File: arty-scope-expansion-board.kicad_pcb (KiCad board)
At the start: 4 copper layers, 109 x 86 mm, 20 parts, among them J1 PMOD_A, J2 PMOD_B, J3 PMOD_C, J4 PMOD_D, U1 AD9288, U2 74LS374, U3 74LS374

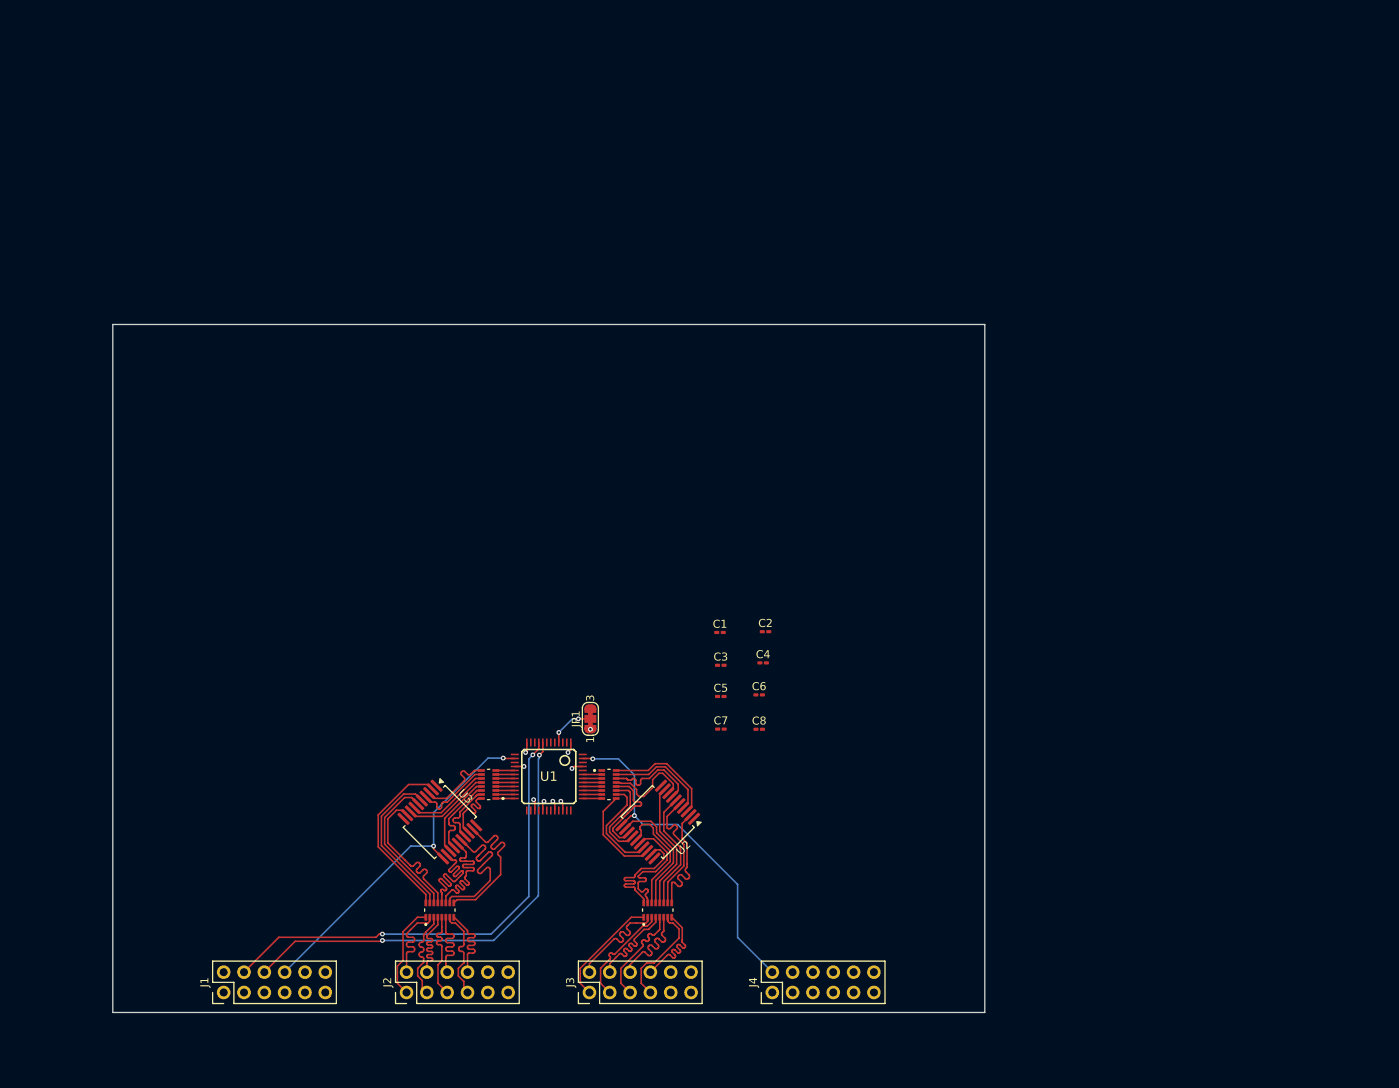
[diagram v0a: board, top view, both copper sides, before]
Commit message: [feat] Added footprints to all A channel elements
TVS diode still doesn't have correct footprint or model. Find one on
LCSC.
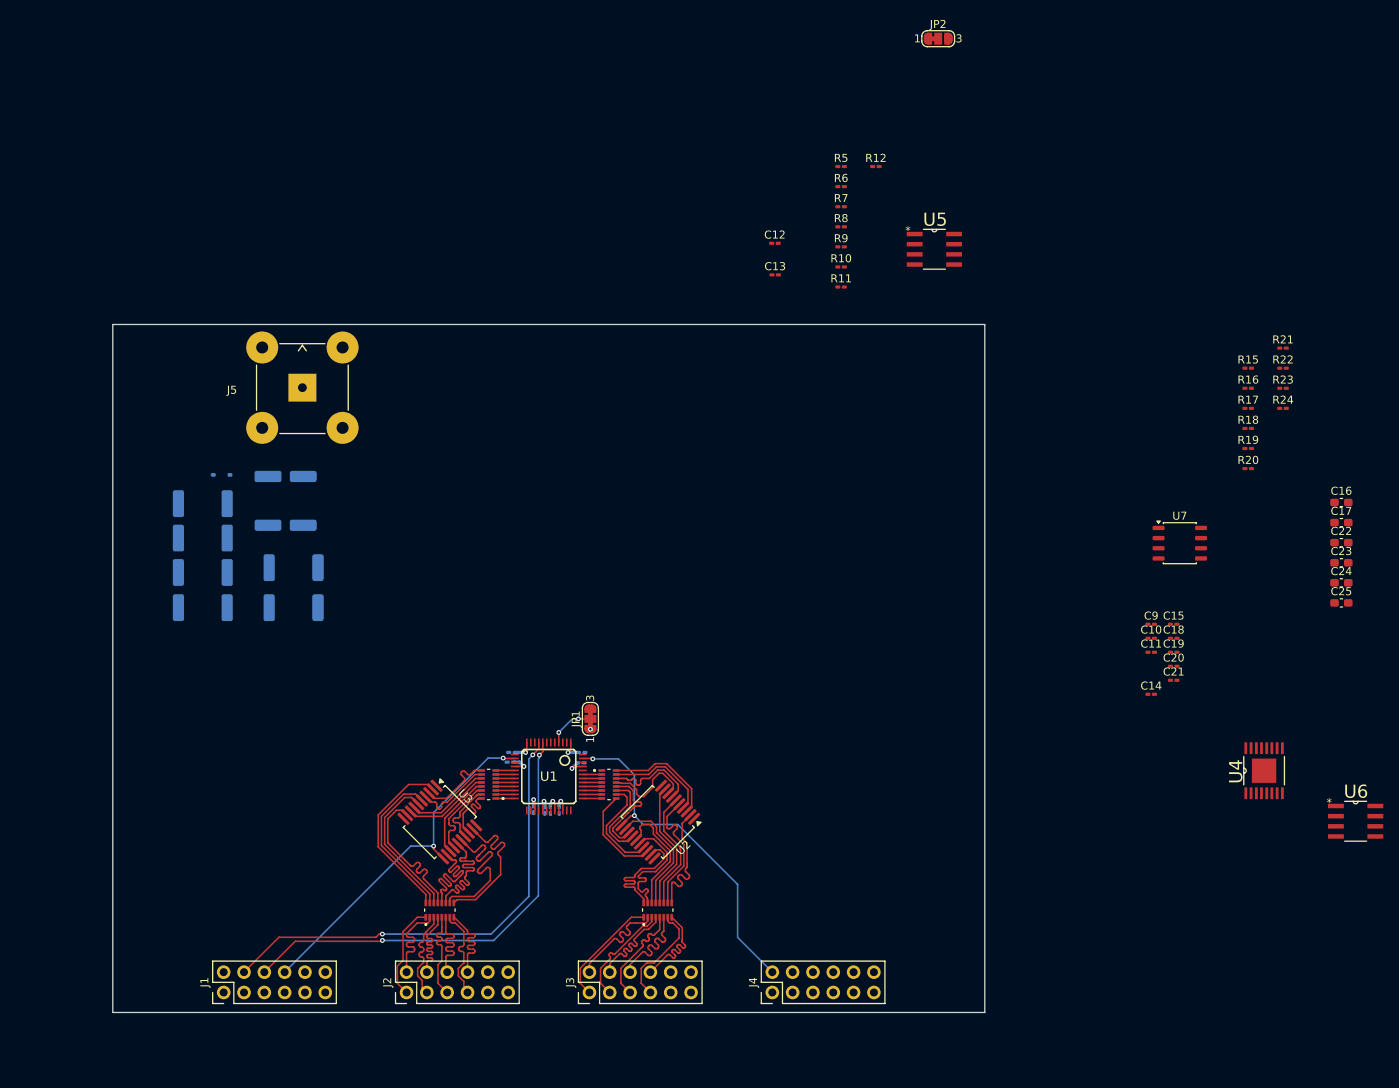
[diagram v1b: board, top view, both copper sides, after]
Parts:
- added C10: 1n, Capacitor_SMD:C_0201_0603Metric_Pad0.64x0.40mm_HandSolder, F.Cu at (245.3, 76.2)
- added C11: 1n, Capacitor_SMD:C_0201_0603Metric_Pad0.64x0.40mm_HandSolder, F.Cu at (245.3, 78.0)
- added C12: 10u, Capacitor_SMD:C_0201_0603Metric_Pad0.64x0.40mm_HandSolder, F.Cu at (198.3, 26.9)
- added C13: 100n, Capacitor_SMD:C_0201_0603Metric_Pad0.64x0.40mm_HandSolder, F.Cu at (198.3, 30.8)
- added C14: 100n, Capacitor_SMD:C_0201_0603Metric_Pad0.64x0.40mm_HandSolder, F.Cu at (245.3, 83.2)
- added C15: 10u, Capacitor_SMD:C_0201_0603Metric_Pad0.64x0.40mm_HandSolder, F.Cu at (248.1, 74.5)
- added C16: 100n, Capacitor_SMD:C_0603_1608Metric_Pad1.08x0.95mm_HandSolder, F.Cu at (269.1, 59.3)
- added C17: 100n, Capacitor_SMD:C_0603_1608Metric_Pad1.08x0.95mm_HandSolder, F.Cu at (269.1, 61.8)
- added C18: 47p, Capacitor_SMD:C_0201_0603Metric_Pad0.64x0.40mm_HandSolder, F.Cu at (248.1, 76.2)
- added C19: 10p, Capacitor_SMD:C_0201_0603Metric_Pad0.64x0.40mm_HandSolder, F.Cu at (248.1, 78.0)
- added C20: 100n, Capacitor_SMD:C_0201_0603Metric_Pad0.64x0.40mm_HandSolder, F.Cu at (248.1, 79.7)
- added C21: 10u, Capacitor_SMD:C_0201_0603Metric_Pad0.64x0.40mm_HandSolder, F.Cu at (248.1, 81.5)
- added C22: 10u, Capacitor_SMD:C_0603_1608Metric_Pad1.08x0.95mm_HandSolder, F.Cu at (269.1, 64.3)
- added C23: 100n, Capacitor_SMD:C_0603_1608Metric_Pad1.08x0.95mm_HandSolder, F.Cu at (269.1, 66.8)
- added C24: 10u, Capacitor_SMD:C_0603_1608Metric_Pad1.08x0.95mm_HandSolder, F.Cu at (269.1, 69.3)
- added C25: 100n, Capacitor_SMD:C_0603_1608Metric_Pad1.08x0.95mm_HandSolder, F.Cu at (269.1, 71.8)
- added C9: 100n, Capacitor_SMD:C_0201_0603Metric_Pad0.64x0.40mm_HandSolder, F.Cu at (245.3, 74.5)
- added D3: SD24C-01F, Diode_SMD:D_SOD-323, B.Cu at (129.1, 55.8)
- added J5: Conn_Coaxial, Connector_Coaxial:BNC_TEConnectivity_1478035_Horizontal, F.Cu at (139.2, 44.9)
- added JP2: Jumper_3_Bridged12, Jumper:SolderJumper-3_P1.3mm_Bridged12_RoundedPad1.0x1.5mm_NumberLabels, F.Cu at (218.7, 1.27)
- added R1: 11, Resistor_SMD:R_2512_6332Metric_Pad1.40x3.35mm_HandSolder, B.Cu at (139.3, 59.0)
- added R10: Rt/2, Resistor_SMD:R_0201_0603Metric_Pad0.64x0.40mm_HandSolder, F.Cu at (206.5, 29.8)
- added R11: 499, Resistor_SMD:R_0201_0603Metric_Pad0.64x0.40mm_HandSolder, F.Cu at (206.5, 32.3)
- added R12: 499, Resistor_SMD:R_0201_0603Metric_Pad0.64x0.40mm_HandSolder, F.Cu at (210.9, 17.3)
- added R13: 11, Resistor_SMD:R_2512_6332Metric_Pad1.40x3.35mm_HandSolder, B.Cu at (134.9, 59.0)
- added R14: 222, Resistor_SMD:R_2512_6332Metric_Pad1.40x3.35mm_HandSolder, B.Cu at (126.8, 59.4)
- added R15: 499, Resistor_SMD:R_0201_0603Metric_Pad0.64x0.40mm_HandSolder, F.Cu at (257.4, 42.5)
- added R16: 499, Resistor_SMD:R_0201_0603Metric_Pad0.64x0.40mm_HandSolder, F.Cu at (257.4, 45.0)
- added R17: 499, Resistor_SMD:R_0201_0603Metric_Pad0.64x0.40mm_HandSolder, F.Cu at (257.4, 47.5)
- added R18: 499, Resistor_SMD:R_0201_0603Metric_Pad0.64x0.40mm_HandSolder, F.Cu at (257.4, 50.0)
- added R19: 100, Resistor_SMD:R_0201_0603Metric_Pad0.64x0.40mm_HandSolder, F.Cu at (257.4, 52.5)
- added R2: 222, Resistor_SMD:R_2512_6332Metric_Pad1.40x3.35mm_HandSolder, B.Cu at (126.8, 72.4)
- added R20: 100, Resistor_SMD:R_0201_0603Metric_Pad0.64x0.40mm_HandSolder, F.Cu at (257.4, 55.0)
- added R21: 2.61k, Resistor_SMD:R_0201_0603Metric_Pad0.64x0.40mm_HandSolder, F.Cu at (261.8, 40.0)
- added R22: 10k, Resistor_SMD:R_0201_0603Metric_Pad0.64x0.40mm_HandSolder, F.Cu at (261.8, 42.5)
- added R23: 49.9, Resistor_SMD:R_0201_0603Metric_Pad0.64x0.40mm_HandSolder, F.Cu at (261.8, 45.0)
- added R24: 49.9, Resistor_SMD:R_0201_0603Metric_Pad0.64x0.40mm_HandSolder, F.Cu at (261.8, 47.5)
- added R25: 222, Resistor_SMD:R_2512_6332Metric_Pad1.40x3.35mm_HandSolder, B.Cu at (126.8, 63.7)
- added R26: 222, Resistor_SMD:R_2512_6332Metric_Pad1.40x3.35mm_HandSolder, B.Cu at (126.8, 68.0)
- added R3: 499, Resistor_SMD:R_2512_6332Metric_Pad1.40x3.35mm_HandSolder, B.Cu at (138.1, 72.4)
- added R4: 55.6, Resistor_SMD:R_2512_6332Metric_Pad1.40x3.35mm_HandSolder, B.Cu at (138.1, 67.4)
- added R5: 100, Resistor_SMD:R_0201_0603Metric_Pad0.64x0.40mm_HandSolder, F.Cu at (206.5, 17.3)
- added R6: 100, Resistor_SMD:R_0201_0603Metric_Pad0.64x0.40mm_HandSolder, F.Cu at (206.5, 19.8)
- added R7: 499, Resistor_SMD:R_0201_0603Metric_Pad0.64x0.40mm_HandSolder, F.Cu at (206.5, 22.3)
- added R8: 499, Resistor_SMD:R_0201_0603Metric_Pad0.64x0.40mm_HandSolder, F.Cu at (206.5, 24.8)
- added R9: Rt, Resistor_SMD:R_0201_0603Metric_Pad0.64x0.40mm_HandSolder, F.Cu at (206.5, 27.3)
- added U4: AD8370AREZ-RL7, inzynierka.Library:SOP65P640X120-17N, F.Cu at (259.4, 92.8)
- added U5: AD8132ARZ, inzynierka.Library:SOIC127P600X175-8N, F.Cu at (218.2, 27.6)
- added U6: AD8132ARZ, inzynierka.Library:SOIC127P600X175-8N, F.Cu at (270.9, 99.1)
- added U7: MCP4822, Package_SO:JEITA_SOIC-8_3.9x4.9mm_P1.27mm, F.Cu at (248.9, 64.3)
- C1, C2, C3, C4, C5, C6, C7, C8: moved to B.Cu
- JP1: value Jumper_3_Bridged12 -> DFS Select
- moved C2 34.9 mm to (170.2, 97.7), turned to 90 degrees
- moved C4 34.0 mm to (168.1, 97.6), turned to 90 degrees
- moved C6 32.2 mm to (165.2, 91.7)
- moved C1 29.9 mm to (171.3, 97.7), turned to 90 degrees
- moved C3 28.5 mm to (169.5, 97.7), turned to 90 degrees
- moved C5 27.0 mm to (165.4, 90.5)
- moved C8 22.7 mm to (174.0, 91.8), turned to 180 degrees
- moved C7 17.7 mm to (174.1, 90.5), turned to 180 degrees
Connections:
- C1 pad 1: VDD -> +3.3VCC
- C2 pad 1: VDD -> +3.3VCC
- C3 pad 1: VDD -> +3.3VCC
- C4 pad 1: VDD -> +3.3VCC
- C5 pad 1: VDD -> +3.3VCC
- C6 pad 1: VDD -> +3.3VCC
- C7 pad 1: VDD -> +3.3VCC
- C8 pad 1: VDD -> +3.3VCC
- J1 pad 1: unconnected-(J1-Pin_1-Pad1) -> PGA_CLK_A
- J1 pad 11: VDD -> +3.3VCC
- J1 pad 12: VDD -> +3.3VCC
- J1 pad 3: unconnected-(J1-Pin_3-Pad3) -> PGA_DATA_A
- J1 pad 5: unconnected-(J1-Pin_5-Pad5) -> PGA_LATCH_A
- J2 pad 11: VDD -> +3.3VCC
- J2 pad 12: VDD -> +3.3VCC
- J3 pad 11: VDD -> +3.3VCC
- J3 pad 12: VDD -> +3.3VCC
- J4 pad 1: unconnected-(J4-Pin_1-Pad1) -> PGA_CLK_B
- J4 pad 11: VDD -> +3.3VCC
- J4 pad 12: VDD -> +3.3VCC
- J4 pad 3: unconnected-(J4-Pin_3-Pad3) -> PGA_DATA_B
- J4 pad 4: unconnected-(J4-Pin_4-Pad4) -> DAC_CS
- J4 pad 5: unconnected-(J4-Pin_5-Pad5) -> PGA_LATCH_B
- J4 pad 6: unconnected-(J4-Pin_6-Pad6) -> DAC_SDI
- J4 pad 7: unconnected-(J4-Pin_7-Pad7) -> DAC_LDAC
- J4 pad 8: unconnected-(J4-Pin_8-Pad8) -> DAC_SCK
- U1 pad 13: VDD -> +3.3VCC
- U1 pad 15: VDD -> +3.3VCC
- U1 pad 2: unconnected-(U1-AINA-Pad2) -> +AINA
- U1 pad 28: VDD -> +3.3VCC
- U1 pad 3: unconnected-(U1-/AINA-Pad3) -> -AINA
- U1 pad 30: VDD -> +3.3VCC
- U1 pad 31: VDD -> +3.3VCC
- U1 pad 33: VDD -> +3.3VCC
- U1 pad 46: VDD -> +3.3VCC
- U1 pad 48: VDD -> +3.3VCC
- U1 pad 5: unconnected-(U1-REFINA-Pad5) -> REFOUT
- U1 pad 6: unconnected-(U1-REFOUT-Pad6) -> REFOUT
- U1 pad 7: unconnected-(U1-REFINB-Pad7) -> REFOUT
- U2 pad 20: +3.3V -> +3.3VCC
- U3 pad 20: +3.3V -> +3.3VCC
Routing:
- net GND: track 10.6 -> 18.8 mm

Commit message: [feat] Started routing A channel input traces
Input 50 Ohm traces still needs routing. Anty aliasing filter needs
checking if values are correct with some simulation software. Still no
power planes. Serial signals for PGA/VGA and DAC needs logic level
shifters from 3.3V FPGA to 5V signals.
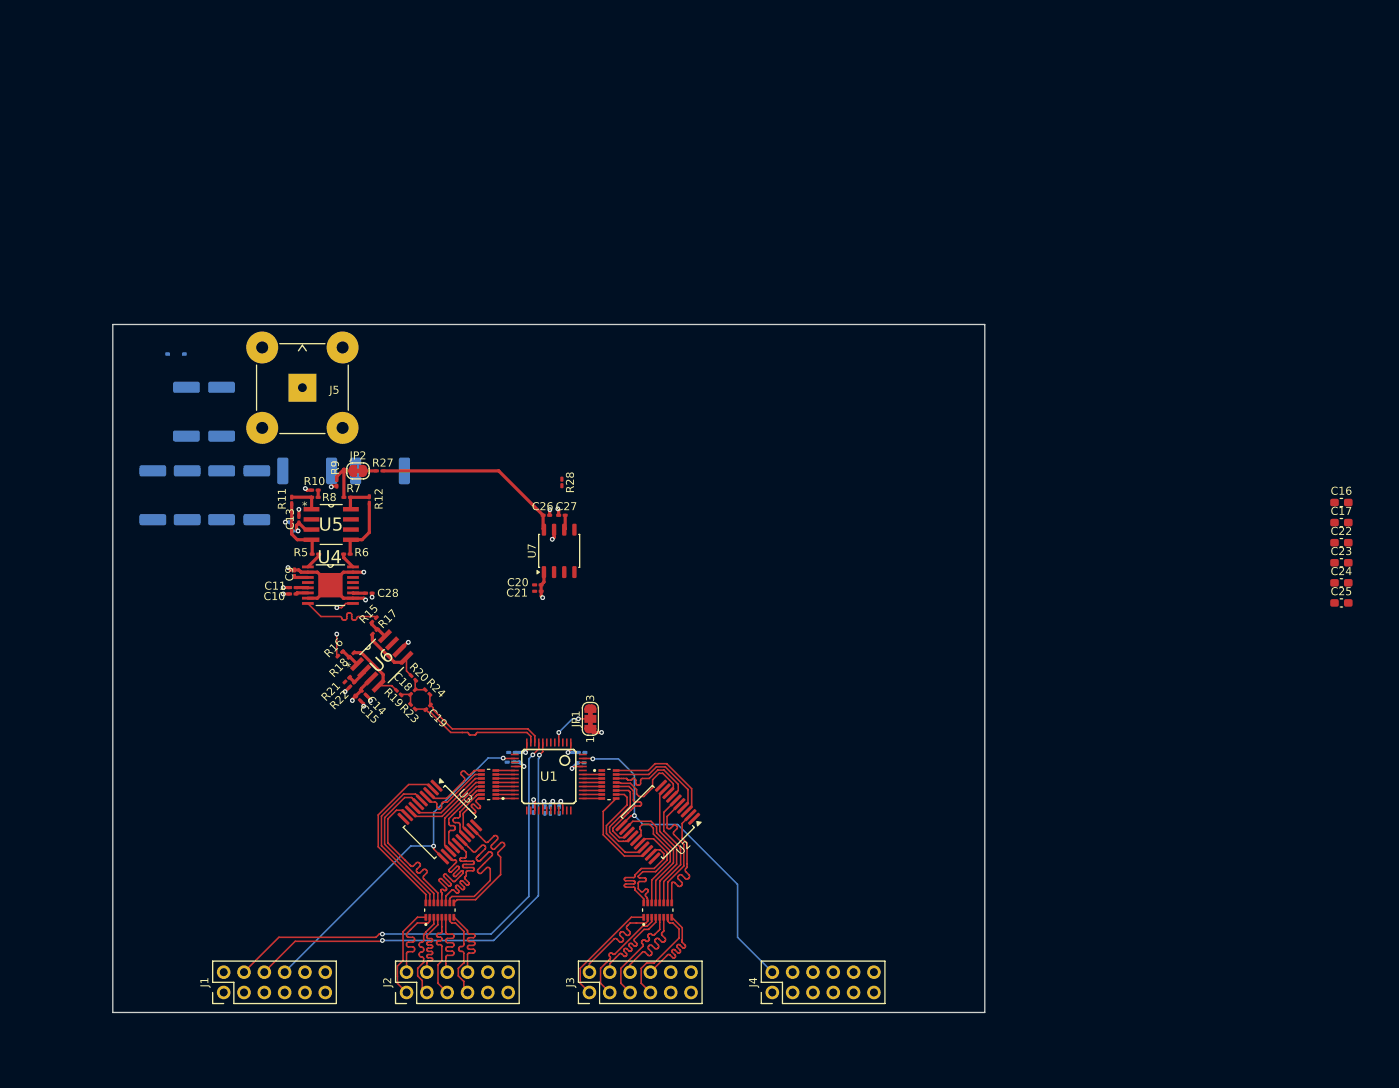
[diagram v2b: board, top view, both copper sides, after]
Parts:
- added C26: 1n, Capacitor_SMD:C_0201_0603Metric_Pad0.64x0.40mm_HandSolder, F.Cu at (169.7, 60.9)
- added C27: 1n, Capacitor_SMD:C_0201_0603Metric_Pad0.64x0.40mm_HandSolder, F.Cu at (171.6, 60.9)
- added C28: 1n, Capacitor_SMD:C_0201_0603Metric_Pad0.64x0.40mm_HandSolder, F.Cu at (147.5, 70.6)
- added R27: 20k, Resistor_SMD:R_0201_0603Metric_Pad0.64x0.40mm_HandSolder, F.Cu at (148.9, 55.3)
- added R28: 20k, Resistor_SMD:R_0201_0603Metric_Pad0.64x0.40mm_HandSolder, F.Cu at (171.6, 56.7)
- C12: moved to B.Cu
- JP2: value Jumper_3_Bridged12 -> Jumper_2_Bridged; footprint Jumper:SolderJumper-3_P1.3mm_Bridged12_RoundedPad1.0x1.5mm_NumberLabels -> Jumper:SolderJumper-2_P1.3mm_Bridged_RoundedPad1.0x1.5mm
- R10: value Rt/2 -> 27.8
- R9: value Rt -> 55.6
- moved R21 124.1 mm to (144.8, 81.4), turned to -135 degrees
- moved U6 123.4 mm to (149.1, 79.1), turned to 45 degrees
- moved R22 122.9 mm to (145.4, 82.0), turned to 45 degrees
- moved U4 119.0 mm to (142.7, 69.6), turned to 0 degrees
- moved R16 118.3 mm to (143.9, 78.2), turned to 45 degrees
- moved R23 115.8 mm to (153.0, 84.8), turned to -45 degrees
- moved R18 115.6 mm to (145.3, 78.3), turned to 45 degrees
- moved R15 113.7 mm to (148.2, 73.9), turned to -135 degrees
- moved R17 112.7 mm to (148.2, 75.4), turned to 45 degrees
- moved R24 112.7 mm to (154.8, 82.9), turned to -45 degrees
- moved R19 110.5 mm to (151.2, 83.0), turned to -45 degrees
- moved C11 107.6 mm to (138.0, 69.9)
- moved R20 107.6 mm to (153.1, 81.2), turned to -45 degrees
- moved C10 107.5 mm to (138.0, 70.7)
- moved C9 107.3 mm to (138.2, 68.1), turned to -90 degrees
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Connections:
- net OPHI_A renamed OP_A+
- net OPLO_A renamed OP_A-
- C19 pad 1: -AINA -> AINA-
- C19 pad 2: +AINA -> AINA+
- JP2 pad 1: GND -> DAC_A
- JP2 pad 2: Net-(JP2-C) -> SIG_A
- R23 pad 2: +AINA -> AINA+
- R24 pad 2: -AINA -> AINA-
- R9 pad 1: Net-(JP2-C) -> GND
- U1 pad 10: unconnected-(U1-/AINB-Pad10) -> AINA-
- U1 pad 11: unconnected-(U1-AINB-Pad11) -> AINA+
- U1 pad 2: +AINA -> unconnected-(U1-AINA-Pad2)
- U1 pad 3: -AINA -> unconnected-(U1-/AINA-Pad3)
- U4 pad 11: +5VCC -> Net-(U4-VCCO)
- U7 pad 6: DAC_B -> Net-(U7-VB)
- U7 pad 8: DAC_A -> Net-(U7-VA)
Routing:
- net GND: track 18.8 -> 52.8 mm, vias 9 -> 26
- net Net-(U7-VA): track 0.00 -> 24.2 mm
- net AINA-: track 0.00 -> 17.0 mm
- net AINA+: track 0.00 -> 17.0 mm
- net +5VCC: track 0.00 -> 14.4 mm, vias 0 -> 3
- net OP_A+: track 0.00 -> 11.2 mm
- net Net-(U6--OUT): track 0.00 -> 9.83 mm
- net Net-(U6-+OUT): track 0.00 -> 8.90 mm
- net Net-(U5-+OUT): track 0.00 -> 8.40 mm
- net OP_A-: track 0.00 -> 8.37 mm, vias 0 -> 2
- net Net-(U5--OUT): track 0.00 -> 8.17 mm
- net SIG_A: track 0.00 -> 6.34 mm
- net Net-(U5--IN): track 0.00 -> 4.00 mm
- net Net-(U5-+IN): track 0.00 -> 3.91 mm
- net REFOUT_VOCM: track 0.00 -> 2.74 mm
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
